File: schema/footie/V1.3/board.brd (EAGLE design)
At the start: 69.5 x 53.3 mm, 42 parts, among them T1 2N3565, U1 24AA32A-I/SN, U2 USD-SOCKETNEW, U3 HC_05, U4 MCP73831, U5 3.3 regulator, U6 ATMEGA328P-AU

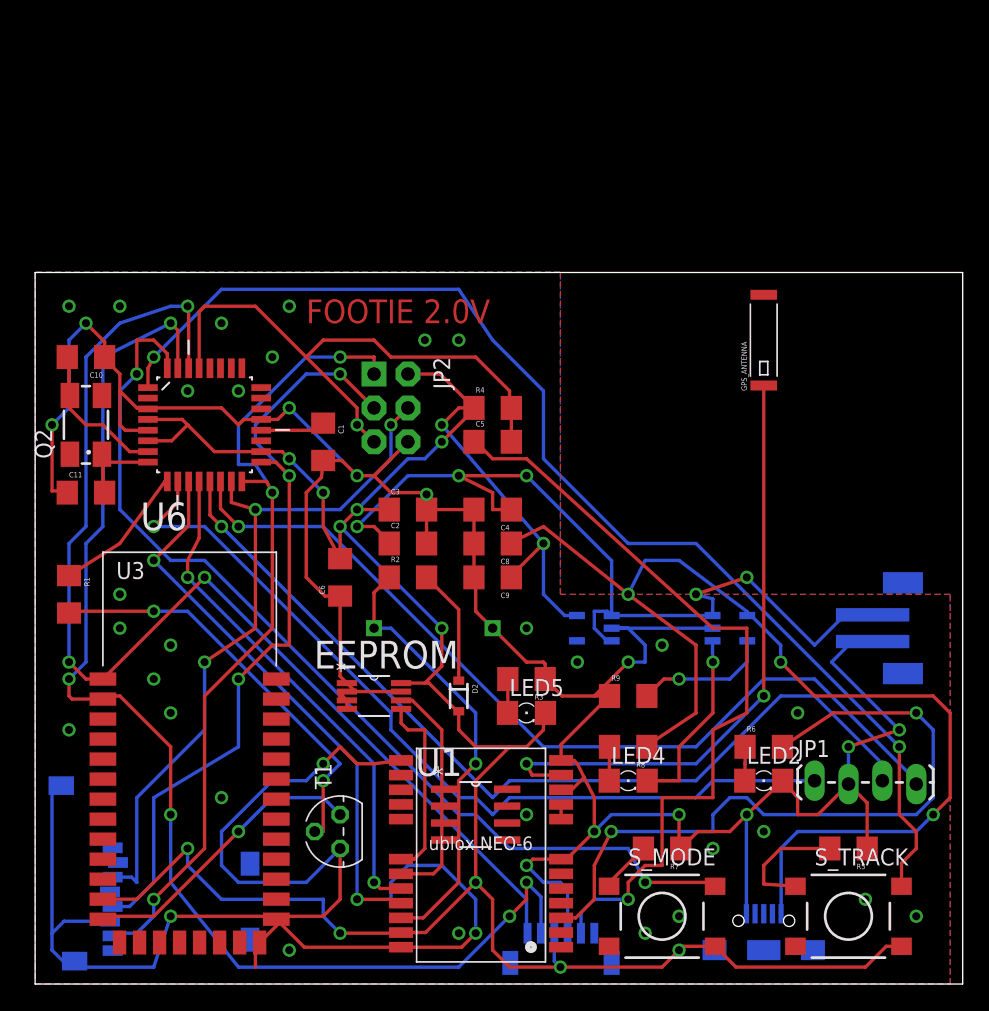
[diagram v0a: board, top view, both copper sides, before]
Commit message: add new schematic add new setting ublox
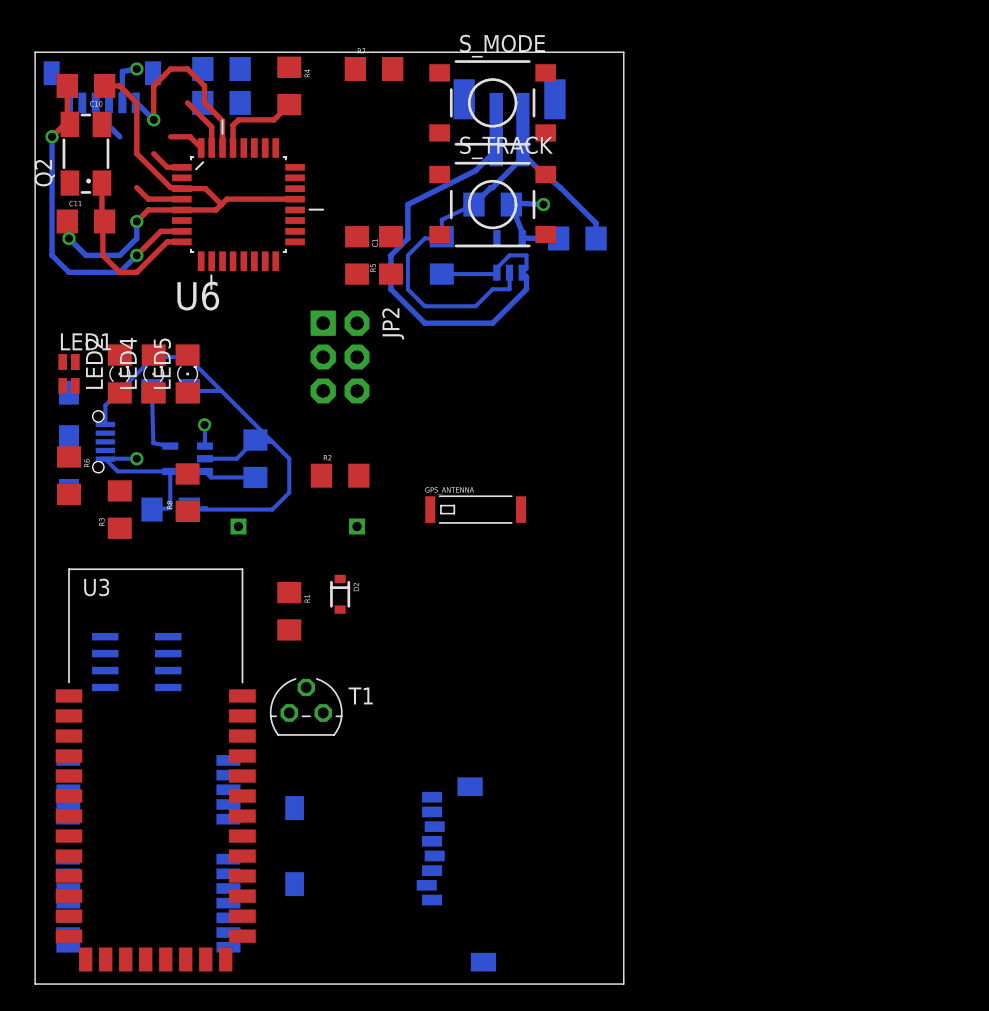
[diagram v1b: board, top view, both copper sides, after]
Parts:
- removed EEPROM: 24LC32A-I/MS, Microchip_By_element14_Batch_1:SOP65P490X110-8N
- removed JP1: (no value), SparkFun-Connectors:1X04_LOCK_LONGPADS
- added LED1: GM1WA55311A, led:GM1WA55311A
- moved U$2 73.3 mm to (5.08, 67.3), turned to 180 degrees
- moved MICRO_USB 64.5 mm to (2.54, 40.6), turned to 180 degrees
- moved R7 62.3 mm to (25.4, 68.6), turned to 0 degrees
- moved S_MODE 62.3 mm to (34.3, 66.0)
- moved S_TRACK 59.6 mm to (34.3, 58.4)
- moved LED2 57.1 mm to (6.35, 45.7), turned to 90 degrees
- moved R5 56.1 mm to (26.7, 54.6), turned to 90 degrees
- moved R6 55.9 mm to (2.54, 38.1), turned to 270 degrees
- moved BATTERY_CONNECTOR 49.0 mm to (35.6, 66.0), turned to 0 degrees
- moved LED4 46.8 mm to (8.89, 45.7), turned to 90 degrees
- moved U4 42.6 mm to (11.4, 39.4), turned to 270 degrees
- moved R9 41.2 mm to (10.2, 44.5), flipped to the bottom
- moved R8 38.1 mm to (11.4, 36.8), turned to 90 degrees
- moved C6 36.7 mm to (14.0, 66.0), flipped to the bottom, turned to 180 degrees
- moved LED5 35.9 mm to (11.4, 45.7), turned to 90 degrees
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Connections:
- net +3V3: no longer EEPROM.8
- net D10: now also LED1.1; no longer JP1.4
- net D6: now also LED1.2; no longer JP1.1
- net D9: now also LED1.3; no longer JP1.3
- net GND: now also LED1.4; no longer EEPROM.1, EEPROM.2, EEPROM.3, EEPROM.4, EEPROM.7, JP1.2
- net SCL: no longer EEPROM.6
- net SDA: no longer EEPROM.5
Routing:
- net GND: track 328.0 -> 112.5 mm, vias 43 -> 2
- net +3V3: track 193.0 -> 14.6 mm, vias 13 -> 1
- net D3: track 89.4 -> 2.53 mm, vias 2 -> 0
- net ARDUINO_TX: track 92.6 -> 7.57 mm, vias 5 -> 1
- net N$2: track 83.8 -> 9.38 mm, vias 3 -> 0
- net ARDUINO_RX: track 87.5 -> 14.5 mm, vias 3 -> 1
- net D2: track 73.9 -> 2.63 mm, vias 2 -> 0
- net D9: track 68.2 -> 0.00 mm, vias 1 -> 0
- net D10: track 67.1 -> 0.00 mm, vias 1 -> 0
- net D6: track 64.4 -> 0.00 mm, vias 1 -> 0
- net SD_MISO: track 62.1 -> 0.00 mm, vias 3 -> 0
- net SD_SCK: track 59.1 -> 0.00 mm, vias 3 -> 0
- net N$13: track 58.9 -> 0.00 mm, vias 1 -> 0
- net SD_MOSI: track 53.6 -> 0.00 mm, vias 3 -> 0
- net N$3: track 53.1 -> 0.00 mm, vias 2 -> 0
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- removed copper zone on layer 1, net GND
- removed copper zone on layer 16, net GND
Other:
- board size 69.5 x 53.3 mm -> 44.1 x 69.8 mm
- board text removed: "FOOTIE 2.0V"
